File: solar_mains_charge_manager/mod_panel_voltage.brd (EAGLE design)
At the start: 26.3 x 25.4 mm, 12 parts, among them Q1 IRF540, X1 22-23-2051, X2 22-23-2021, X3 22-23-2021, X4 22-23-2021

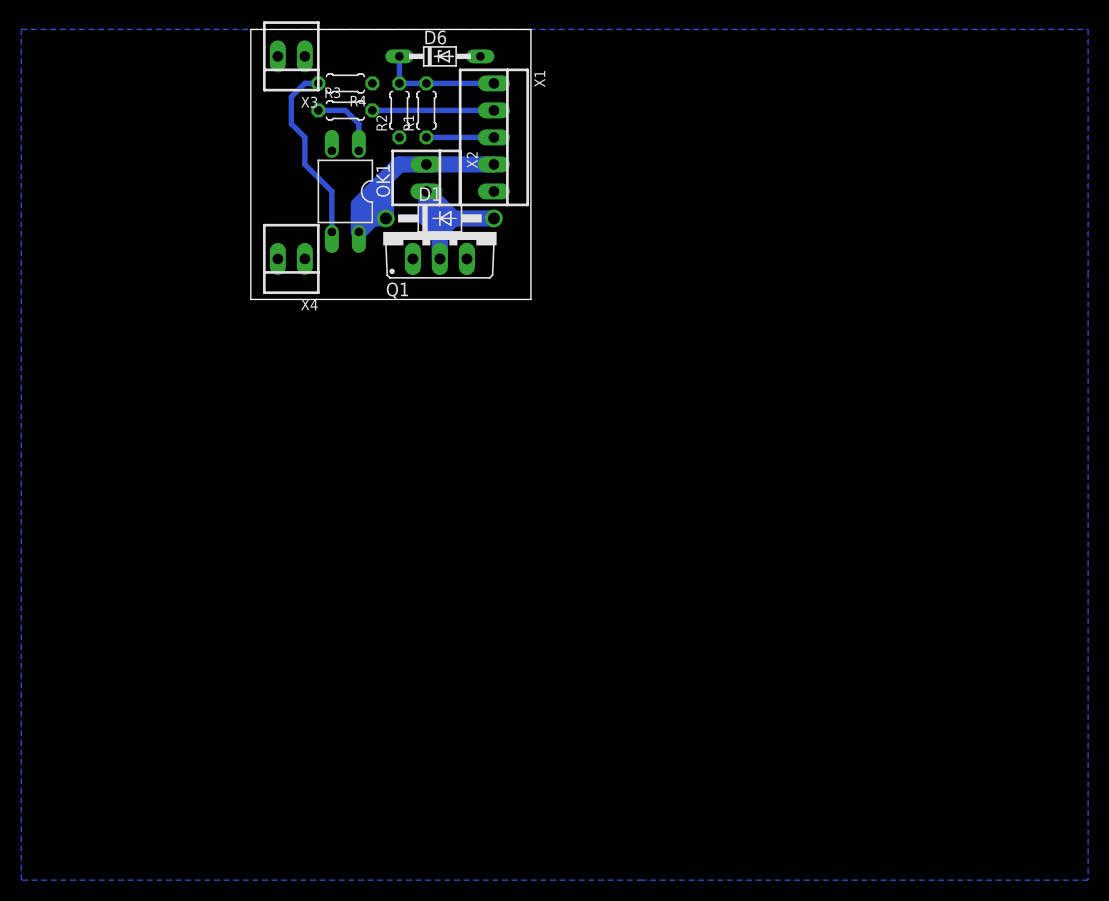
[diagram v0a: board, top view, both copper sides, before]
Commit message: Finished board layout of mod_switch_battery_voltage and more work on psu_considerations.ods
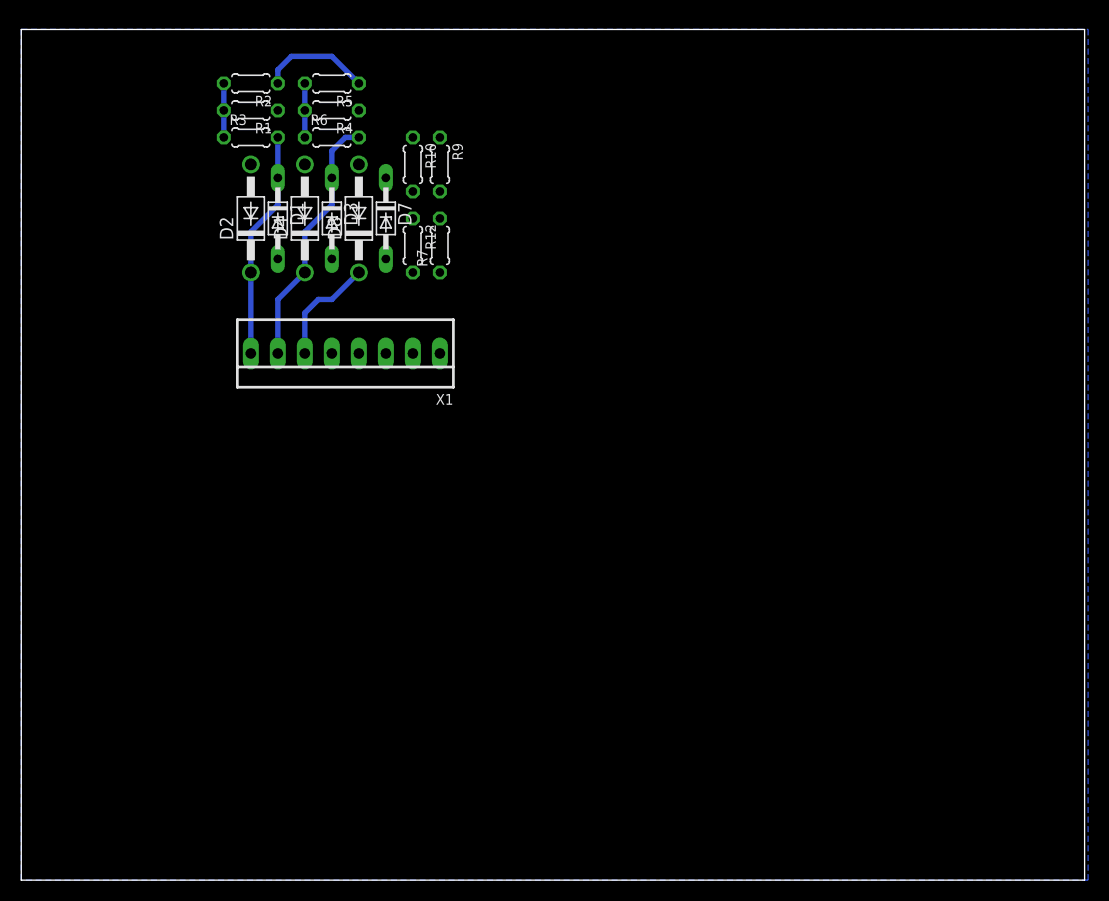
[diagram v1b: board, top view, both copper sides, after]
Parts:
- removed D6: (no value), diode:DO34Z7
- removed OK1: PC817, optocoupler:DIL04
- removed Q1: IRF540, transistor-power:TO220BV
- removed X2, X3, X4: 22-23-2021, con-molex:22-23-2021
- added D2, D4, D8: 1N4004, diode:DO41-10
- added D3, D7: (no value), diode:DO34Z7
- added R10, R12, R5, R6, R7, R9: (no value), resistor:0204/5
- D1: value 1N4004 -> (none); device diode:DO41-10 -> diode:DO34Z7
- X1: value 22-23-2051 -> 22-23-2081; device con-molex:22-23-2051 -> con-molex:22-23-2081
- moved X1 24.7 mm to (30.5, 49.5), turned to 180 degrees
- moved R1 16.5 mm to (21.6, 72.4), turned to 180 degrees
- moved D1 15.2 mm to (24.1, 62.2), turned to 270 degrees
- moved R2 14.2 mm to (21.6, 74.9), turned to 180 degrees
- moved R3 9.25 mm to (21.6, 69.8)
- moved R4 2.84 mm to (29.2, 72.4)
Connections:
- removed net 12V: D1.C, OK1.4, X1.4, X2.1
- removed net BAT: R1.1, X1.3
- removed net N$4: OK1.1, R3.1
- removed net N$43: D6.C, R1.2, R2.2, X1.1
- removed net N$6: R3.2, X1.2
- removed net N$7: OK1.3, Q1.G, R4.2
- new net ADC1: D3.C, D4.C, R6.2, X1.7
- new net ADC2: D1.C, D2.C, R3.2, X1.8
- new net ADC3: D7.C, D8.C, R12.2, X1.6
- new net N$2: R10.2, R12.1, R7.2, R9.2
- new net N$9: R4.2, R5.2, R6.1
- new net P+: R2.1, R5.1, X1.3
- new net P-: R10.1, R4.1, X1.2
- new net VCOMP: R7.1, X1.5
- net GND: now also D1.A, D2.A, D3.A, D4.A, D7.A, D8.A, R1.1, R9.1, X1.1, X1.4; no longer D6.A, OK1.2, Q1.S, R2.1, R4.1, X1.5, X3.1, X3.2, X4.1, X4.2
- net N$5: now also R1.2, R2.2, R3.1; no longer D1.A, Q1.D, X2.2
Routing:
- net 12V: track 28.0 -> 0.00 mm
- net ADC1: track 0.00 -> 24.2 mm
- net ADC2: track 0.00 -> 21.4 mm
- net N$7: track 17.3 -> 0.00 mm
- net N$5: track 21.2 -> 5.08 mm
- net N$6: track 11.4 -> 0.00 mm
- net N$43: track 11.4 -> 0.00 mm
- net ADC3: track 0.00 -> 10.5 mm
- net P+: track 0.00 -> 10.5 mm
- net N$4: track 6.88 -> 0.00 mm
- net BAT: track 6.35 -> 0.00 mm
- net N$9: track 0.00 -> 5.08 mm
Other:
- board size 26.3 x 25.4 mm -> 100 x 80 mm
